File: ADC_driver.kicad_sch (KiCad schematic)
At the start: 21 parts, among them U1 ADA4930-2YCPZ-R2

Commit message: updated the resistor sizings from all 0805 to 0402, 0603 and 0805s, to match the thunderscope directly
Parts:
- removed C104_1, C104_2, C105_1, C70_1, C70_2: 1uF, Thunderscope_Rev5:GEN_C_0402, symbol Thunderscope_Rev5:CAP 1uF 25V X5R 0402
- removed C69_1: 10uF, Thunderscope_Rev5:GEN_C_0603, symbol Thunderscope_Rev5:CAP 10uF 25V X5R 0603
- added C124, C125, C126, C127, C128: 1uF, Capacitor_SMD:C_0402_1005Metric_Pad0.74x0.62mm_HandSolder, symbol Device:C
- added C129: 10uF, Capacitor_SMD:C_0402_1005Metric_Pad0.74x0.62mm_HandSolder, symbol Device:C
- R1, R2: footprint Resistor_SMD:R_01005_0402Metric_Pad0.57x0.30mm_HandSolder -> Resistor_SMD:R_0402_1005Metric_Pad0.72x0.64mm_HandSolder
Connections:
- net +3V3_ACQ: now also C126.1, C127.1, C128.1, C129.1
- net GND: now also C124.2, C125.2, C126.2, C127.2, C128.2, C129.2
- net VCM1: now also C125.1
- net VCM2: now also C124.1

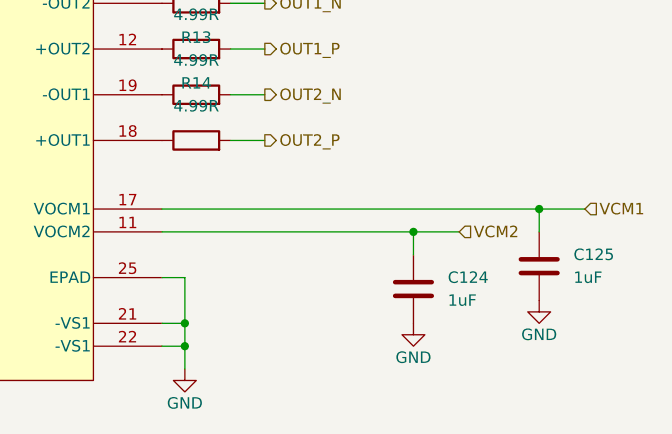
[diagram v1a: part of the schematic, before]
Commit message: schematic complete. no ERC errors
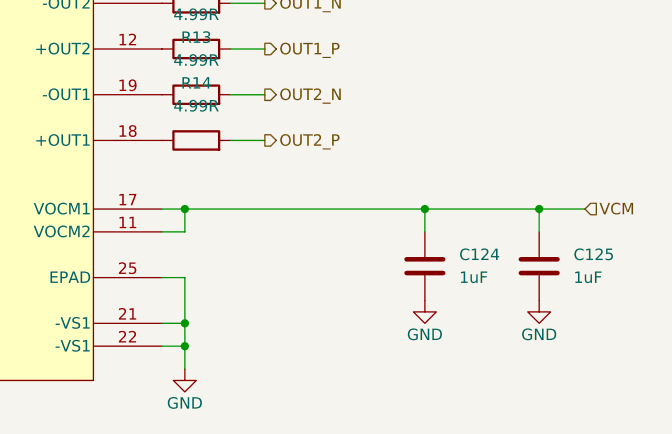
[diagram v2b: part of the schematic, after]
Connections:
- net GND: now also C124.1; no longer C124.2
- net VCM1 renamed VCM
- net VCM: now also C124.2, U1.11 (VOCM2)
- removed net VCM2: C124.1, U1.11 (VOCM2)
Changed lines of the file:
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@@
+	)
+	(junction
+		(at 190.5 111.76)
+		(diameter 0)
+		(color 0 0 0 0)
 	)
 	(junction
@@
 	)
 	(junction
+		(at 163.83 111.76)
+		(diameter 0)
+		(color 0 0 0 0)
+	)
+	(junction
 		(at 203.2 111.76)
 		(diameter 0)
@@
 	)
 	(junction
-		(at 189.23 114.3)
-		(diameter 0)
-		(color 0 0 0 0)
-	)
-	(junction
 		(at 121.92 50.8)
 		(diameter 0)
@@
 	(wire
 		(pts
-			(xy 189.23 114.3) (xy 194.31 114.3)
-		)
-		(stroke
-			(width 0)
-			(type default)
-		)
-	)
-	(wire
-		(pts
 			(xy 109.22 107.95) (xy 124.46 107.95)
 		)
@@
 	(wire
 		(pts
+			(xy 163.83 114.3) (xy 163.83 111.76)
+		)
+		(stroke
+			(width 0)
+			(type default)
+		)
+	)
+	(wire
+		(pts
 			(xy 163.83 127) (xy 163.83 129.54)
 		)
@@
 	(wire
 		(pts
-			(xy 161.29 114.3) (xy 189.23 114.3)
-		)
-		(stroke
-			(width 0)
-			(type default)
-		)
-	)
-	(wire
-		(pts
 			(xy 111.76 95.25) (xy 109.22 95.25)
 		)
@@
 	(wire
 		(pts
-			(xy 189.23 114.3) (xy 189.23 116.84)
-		)
-		(stroke
-			(width 0)
-			(type default)
-		)
-	)
-	(wire
-		(pts
 			(xy 80.01 50.8) (xy 92.71 50.8)
 		)
@@
 	(wire
 		(pts
+			(xy 161.29 114.3) (xy 163.83 114.3)
+		)
+		(stroke
+			(width 0)
+			(type default)
+		)
+	)
+	(wire
+		(pts
 			(xy 121.92 124.46) (xy 124.46 124.46)
 		)
@@
 	(wire
 		(pts
-			(xy 161.29 111.76) (xy 203.2 111.76)
+			(xy 161.29 111.76) (xy 163.83 111.76)
 		)
 		(stroke
@@
 	(wire
 		(pts
+			(xy 190.5 111.76) (xy 190.5 114.3)
+		)
+		(stroke
+			(width 0)
+			(type default)
+		)
+	)
+	(wire
+		(pts
 			(xy 86.36 92.71) (xy 92.71 92.71)
 		)
@@
 	(wire
 		(pts
+			(xy 190.5 111.76) (xy 203.2 111.76)
+		)
+		(stroke
+			(width 0)
+			(type default)
+		)
+	)
+	(wire
+		(pts
 			(xy 119.38 102.87) (xy 124.46 102.87)
 		)
@@
 		(pts
 			(xy 119.38 80.01) (xy 124.46 80.01)
+		)
+		(stroke
+			(width 0)
+			(type default)
+		)
+	)
+	(wire
+		(pts
+			(xy 163.83 111.76) (xy 190.5 111.76)
 		)
 		(stroke
@@
 		)
 	)
-	(hierarchical_label "VCM1"
+	(hierarchical_label "VCM"
 		(shape input)
 		(at 208.28 111.76 0)
@@
 		)
 	)
-	(hierarchical_label "VCM2"
-		(shape input)
-		(at 194.31 114.3 0)
-		(effects
-			(font
-				(size 1.27 1.27)
-			)
-			(justify left)
-		)
-	)
 	(hierarchical_label "IN1_N"
 		(shape input)
@@
 	(symbol
 		(lib_id "power:GND")
-		(at 189.23 124.46 0)
-		(unit 1)
-		(exclude_from_sim no)
-		(in_bom yes)
-		(on_board yes)
-		(dnp no)
-		(property "Reference" "#PWR01"
-			(at 189.23 130.81 0)
-			(effects
-				(font
-					(size 1.27 1.27)
-				)
-				(hide yes)
-			)
-		)
-		(property "Value" "GND"
-			(at 189.23 128.27 0)
-			(effects
-				(font
-					(size 1.27 1.27)
-				)
-			)
-		)
-		(property "Footprint" ""
-			(at 189.23 124.46 0)
-			(effects
-				(font
-					(size 1.27 1.27)
-				)
-				(hide yes)
-			)
-		)
-		(property "Datasheet" ""
-			(at 189.23 124.46 0)
-			(effects
-				(font
-					(size 1.27 1.27)
-				)
-				(hide yes)
-			)
-		)
-		(property "Description" "Power symbol creates a global label with name \"GND\" , ground"
-			(at 189.23 124.46 0)
-			(effects
-				(font
-					(size 1.27 1.27)
-				)
-				(hide yes)
-			)
-		)
-		(pin "1"
-		)
-		(instances
-			(project "thunderscope-lite"
-				(path "/920a8b65-6ec2-414c-bfee-6322de42233d/2aaae1fd-0637-4070-bb0f-0c0b65ef82d4"
-					(reference "#PWR01")
-					(unit 1)
-				)
-			)
-		)
-	)
-	(symbol
-		(lib_id "power:GND")
 		(at 163.83 129.54 0)
 		(unit 1)
@@
 	(symbol
 		(lib_id "Device:C")
-		(at 189.23 120.65 0)
+		(at 190.5 118.11 180)
 		(unit 1)
 		(exclude_from_sim no)
@@
 		(fields_autoplaced yes)
 		(property "Reference" "C124"
-			(at 193.04 119.3799 0)
-			(effects
-				(font
-					(size 1.27 1.27)
-				)
-				(justify left)
+			(at 194.31 116.8399 0)
+			(effects
+				(font
+					(size 1.27 1.27)
+				)
+				(justify right)
 			)
 		)
 		(property "Value" "1uF"
-			(at 193.04 121.9199 0)
-			(effects
-				(font
-					(size 1.27 1.27)
-				)
-				(justify left)
+			(at 194.31 119.3799 0)
+			(effects
+				(font
+					(size 1.27 1.27)
+				)
+				(justify right)
 			)
 		)
 		(property "Footprint" "Capacitor_SMD:C_0402_1005Metric_Pad0.74x0.62mm_HandSolder"
-			(at 190.1952 124.46 0)
+			(at 189.5348 114.3 0)
 			(effects
 				(font
@@
 		)
 		(property "Datasheet" "~"
-			(at 189.23 120.65 0)
+			(at 190.5 118.11 0)
 			(effects
 				(font
@@
 		)
 		(property "Description" "Unpolarized capacitor"
-			(at 189.23 120.65 0)
+			(at 190.5 118.11 0)
 			(effects
 				(font
@@
 					(unit 1)
 				)
+			)
+		)
+	)
+	(symbol
+		(lib_id "power:GND")
+		(at 190.5 121.92 0)
+		(unit 1)
+		(exclude_from_sim no)
+		(in_bom yes)
+		(on_board yes)
+		(dnp no)
+		(property "Reference" "#PWR01"
+			(at 190.5 128.27 0)
+			(effects
+				(font
+					(size 1.27 1.27)
+				)
+				(hide yes)
+			)
+		)
+		(property "Value" "GND"
+			(at 190.5 125.73 0)
+			(effects
+				(font
+					(size 1.27 1.27)
+				)
+			)
+		)
+		(property "Footprint" ""
+			(at 190.5 121.92 0)
+			(effects
+				(font
+					(size 1.27 1.27)
+				)
+				(hide yes)
+			)
+		)
+		(property "Datasheet" ""
+			(at 190.5 121.92 0)
+			(effects
+				(font
+					(size 1.27 1.27)
+				)
+				(hide yes)
+			)
+		)
+		(property "Description" "Power symbol creates a global label with name \"GND\" , ground"
+			(at 190.5 121.92 0)
+			(effects
+				(font
+					(size 1.27 1.27)
+				)
+				(hide yes)
+			)
+		)
+		(pin "1"
+		)
+		(instances
+			(project "thunderscope-lite"
+				(path "/920a8b65-6ec2-414c-bfee-6322de42233d/2aaae1fd-0637-4070-bb0f-0c0b65ef82d4"
+					(reference "#PWR01")
+					(unit 1)
+				)
